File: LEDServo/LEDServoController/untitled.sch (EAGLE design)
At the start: 9 parts, among them U1 ATTINY2313A

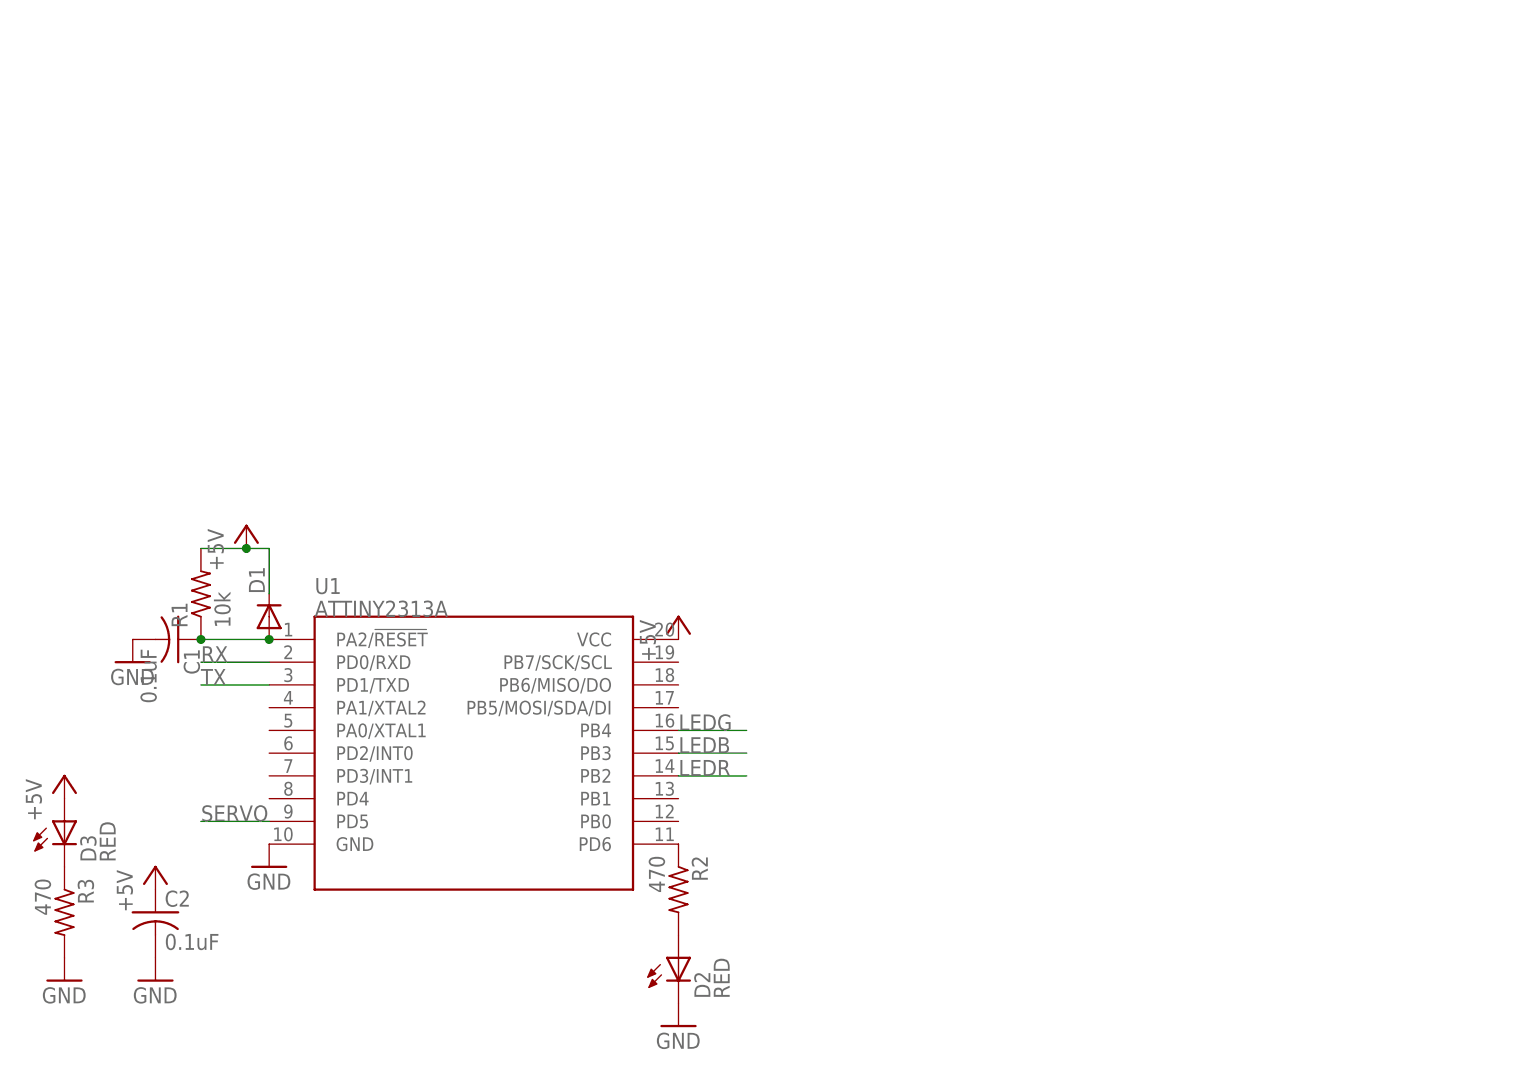
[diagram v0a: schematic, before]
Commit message: LED tested
LED timers tested, RGB and Servo (scope test).  Need to test UART.
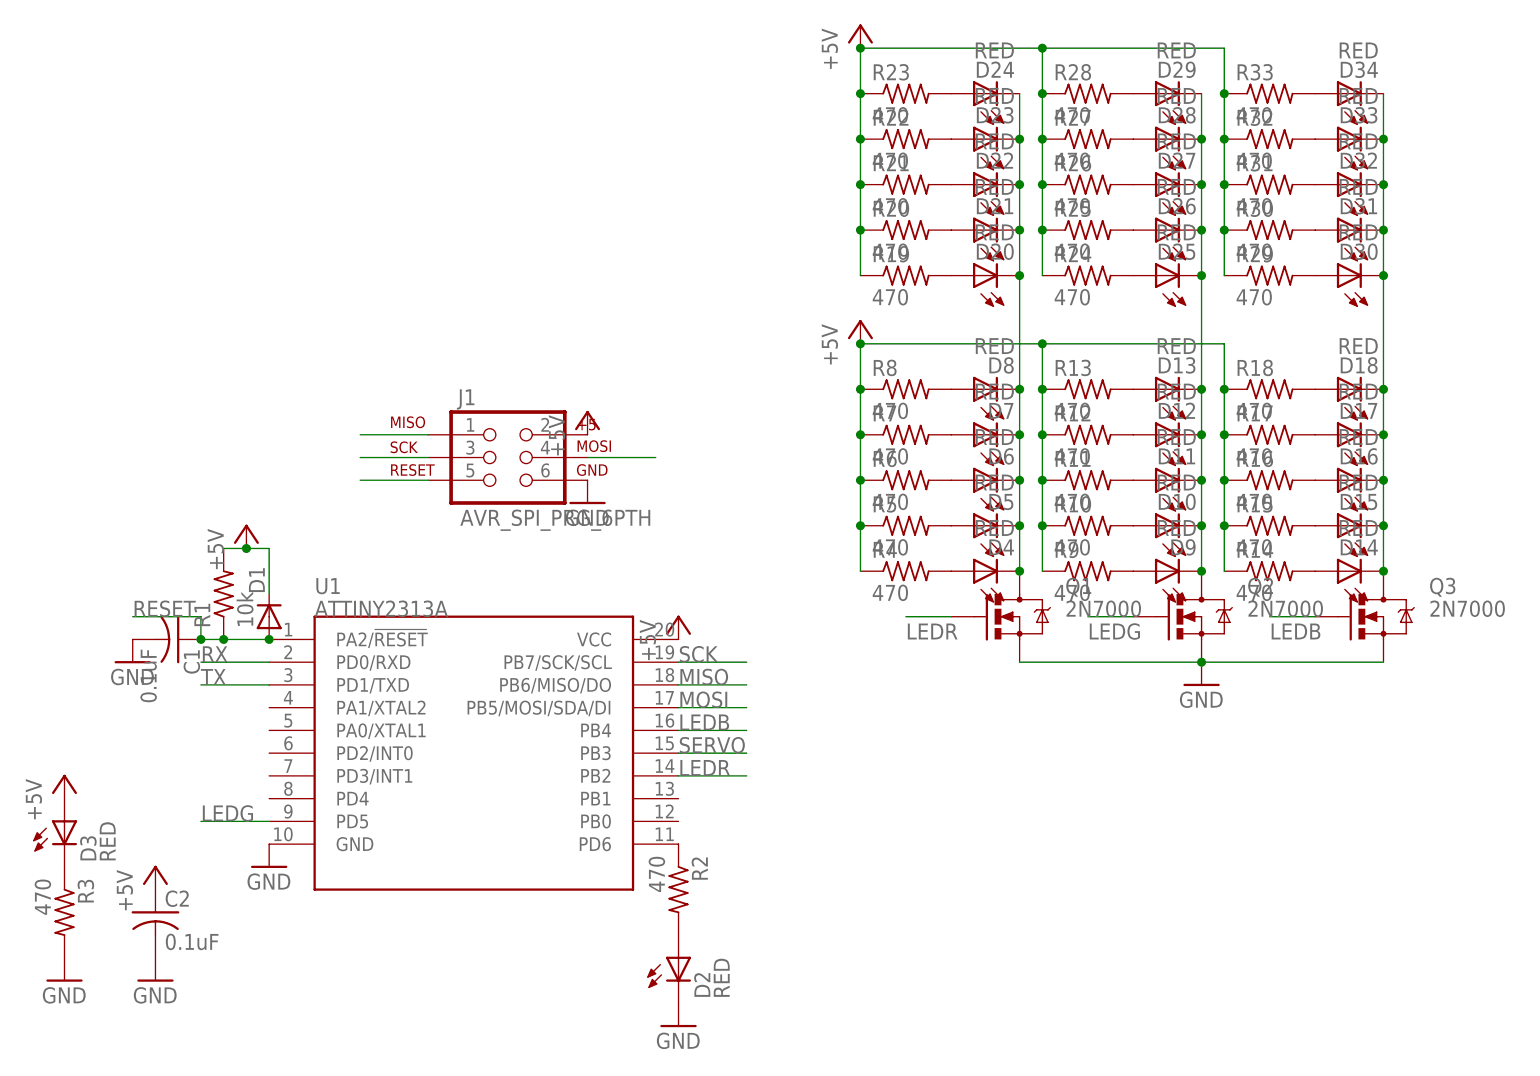
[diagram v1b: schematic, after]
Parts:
- added D10, D11, D12, D13, D14, D15, D16, D17, D18, D20, D21, D22, D23, D24, D25, D26, D27, D28, D29, D30, D31, D32, D33, D34, D4, D5, D6, D7, D8, D9: RED, SparkFun-LED:LED-RED0603
- added J1: AVR_SPI_PRG_6PTH, SparkFun-Connectors:AVR_SPI_PRG_6PTH
- added Q1, Q2, Q3: 2N7000, SparkFun-DiscreteSemi:MOSFET-NCHANNEL2N7000
- added R10, R11, R12, R13, R14, R15, R16, R17, R18, R19, R20, R21, R22, R23, R24, R25, R26, R27, R28, R29, R30, R31, R32, R33, R4, R5, R6, R7, R8, R9: 470, rcl:R-US_0207/10
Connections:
- removed net N$2: C1.1, D1.A, R1.1, U1.PA2/!RESET
- new net MISO: J1.1, U1.PB6/MISO/DO
- new net MOSI: J1.4, U1.PB5/MOSI/SDA/DI
- new net N$10: D7.A, R7.2
- new net N$11: D8.A, R8.2
- new net N$12: D9.A, R9.2
- new net N$13: D10.A, R10.2
- new net N$14: D11.A, R11.2
- new net N$15: D12.A, R12.2
- new net N$16: D13.A, R13.2
- new net N$17: D14.A, R14.2
- new net N$18: D15.A, R15.2
- new net N$19: D16.A, R16.2
- new net N$20: D17.A, R17.2
- new net N$21: D18.A, R18.2
- new net N$26: D10.C, D11.C, D12.C, D13.C, D25.C, D26.C, D27.C, D28.C, D29.C, D9.C, Q2.D
- new net N$27: D14.C, D15.C, D16.C, D17.C, D18.C, D30.C, D31.C, D32.C, D33.C, D34.C, Q3.D
- new net N$28: D20.A, R19.2
- new net N$29: D21.A, R20.2
- new net N$30: D22.A, R21.2
- new net N$31: D23.A, R22.2
- new net N$32: D24.A, R23.2
- new net N$33: D25.A, R24.2
- new net N$34: D26.A, R25.2
- new net N$35: D27.A, R26.2
- new net N$36: D28.A, R27.2
- new net N$37: D29.A, R28.2
- new net N$38: D30.A, R29.2
- new net N$39: D31.A, R30.2
- new net N$40: D32.A, R31.2
- new net N$41: D33.A, R32.2
- new net N$42: D34.A, R33.2
- new net N$43: D20.C, D21.C, D22.C, D23.C, D24.C, D4.C, D5.C, D6.C, D7.C, D8.C, Q1.D
- new net N$7: D4.A, R4.2
- new net N$8: D5.A, R5.2
- new net N$9: D6.A, R6.2
- new net RESET: C1.1, D1.A, J1.5, R1.1, U1.PA2/!RESET
- new net SCK: J1.3, U1.PB7/SCK/SCL
- net +5V: now also J1.2, R10.1, R11.1, R12.1, R13.1, R14.1, R15.1, R16.1, R17.1, R18.1, R19.1, R20.1, R21.1, R22.1, R23.1, R24.1, R25.1, R26.1, R27.1, R28.1, R29.1, R30.1, R31.1, R32.1, R33.1, R4.1, R5.1, R6.1, R7.1, R8.1, R9.1
- net GND: now also J1.6, Q1.S, Q2.S, Q3.S
- net LEDB: now also Q3.G, U1.PB4; no longer U1.PB3
- net LEDG: now also Q2.G, U1.PD5; no longer U1.PB4
- net LEDR: now also Q1.G
- net SERVO: now also U1.PB3; no longer U1.PD5
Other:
- moved on the sheet: R1
